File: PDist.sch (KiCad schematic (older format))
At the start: 2 parts

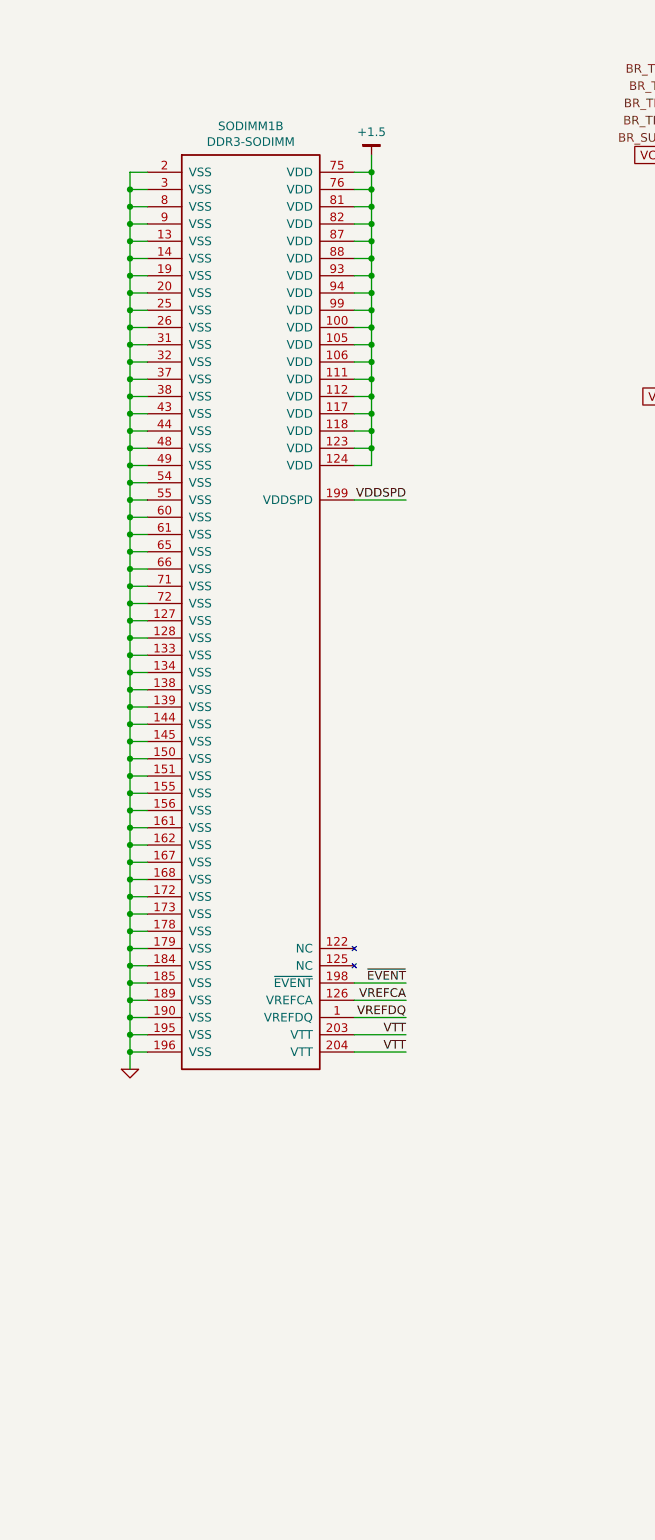
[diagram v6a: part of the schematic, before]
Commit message: Reroute SDRAM after bank swap
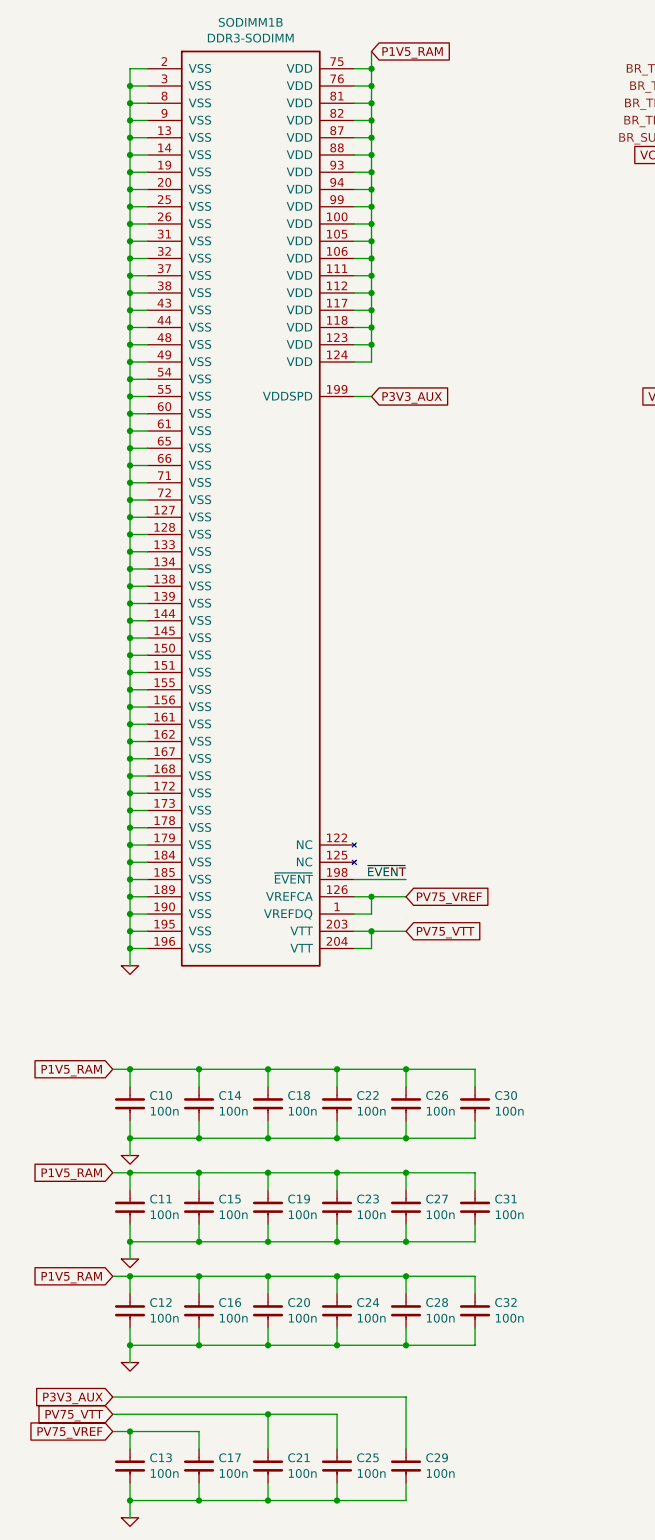
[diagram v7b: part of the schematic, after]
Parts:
- added C10, C11, C12, C13, C14, C15, C16, C17, C18, C19, C20, C21, C22, C23, C24, C25, C26, C27, C28, C29, C30, C31, C32: 100n, IPC7351-Nominal:CAPC1005X55, symbol C-0402
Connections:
- net VREFDQ is gone; now on net PV75_VREF: SODIMM1.1 (VREFDQ)
- net GND: now also C10.2, C11.2, C12.2, C13.2, C14.2, C15.2, C16.2, C17.2, C18.2, C19.2, C20.2, C21.2, C22.2, C23.2, C24.2, C25.2, C26.2, C27.2, C28.2, C29.2, C30.2, C31.2, C32.2
- net +1.5 renamed P1V5_RAM
- net P1V5_RAM: now also C10.1, C11.1, C12.1, C14.1, C15.1, C16.1, C18.1, C19.1, C20.1, C22.1, C23.1, C24.1, C26.1, C27.1, C28.1, C30.1, C31.1, C32.1
- net VDDSPD renamed P3V3_AUX
- net P3V3_AUX: now also C29.1
- net VREFCA renamed PV75_VREF
- net PV75_VREF: now also C13.1, C17.1
- net VTT renamed PV75_VTT
- net PV75_VTT: now also C21.1, C25.1
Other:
- moved on the sheet: SODIMM1B

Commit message: workworkwork
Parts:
- added CPU0, CPU1: XC6SLX25-FGG484, manuf:XILINX-FGG484, symbol XC6SLX25-FGG484
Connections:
- net GND: now also CPU0.A1 (GND), CPU0.A22 (GND), CPU0.AA13 (GND), CPU0.AA17 (GND), CPU0.AA5 (GND), CPU0.AA9 (GND), CPU0.AB1 (GND), CPU0.AB22 (GND), CPU0.B13 (GND), CPU0.B17 (GND), CPU0.B5 (GND), CPU0.B9 (GND), CPU0.D18 (GND), CPU0.D4 (GND), CPU0.E11 (GND), CPU0.E15 (GND), CPU0.E2 (GND), CPU0.E21 (GND), CPU0.E7 (GND), CPU0.G18 (GND), CPU0.G5 (GND), CPU0.H7 (GND), CPU0.J11 (GND), CPU0.J13 (GND), CPU0.J15 (GND), CPU0.J2 (GND), CPU0.J21 (GND), CPU0.J9 (GND), CPU0.K10 (GND), CPU0.K12 (GND), CPU0.K14 (GND), CPU0.L11 (GND), CPU0.L13 (GND), CPU0.L18 (GND), CPU0.L5 (GND), CPU0.L9 (GND), CPU0.M10 (GND), CPU0.M12 (GND), CPU0.M14 (GND), CPU0.N11 (GND), CPU0.N13 (GND), CPU0.N17 (GND), CPU0.N2 (GND), CPU0.N21 (GND), CPU0.N9 (GND), CPU0.P10 (GND), CPU0.P12 (GND), CPU0.P14 (GND), CPU0.R18 (GND), CPU0.R5 (GND), CPU0.U2 (GND), CPU0.U21 (GND), CPU0.U7 (GND), CPU0.V10 (GND), CPU0.V14 (GND), CPU0.V4 (GND), CPU0.W16 (GND), CPU0.W19 (GND), CPU0.W7 (GND), CPU1.A1 (GND), CPU1.A22 (GND), CPU1.AA13 (GND), CPU1.AA17 (GND), CPU1.AA5 (GND), CPU1.AA9 (GND), CPU1.AB1 (GND), CPU1.AB22 (GND), CPU1.B13 (GND), CPU1.B17 (GND), CPU1.B5 (GND), CPU1.B9 (GND), CPU1.D18 (GND), CPU1.D4 (GND), CPU1.E11 (GND), CPU1.E15 (GND), CPU1.E2 (GND), CPU1.E21 (GND), CPU1.E7 (GND), CPU1.G18 (GND), CPU1.G5 (GND), CPU1.H7 (GND), CPU1.J11 (GND), CPU1.J13 (GND), CPU1.J15 (GND), CPU1.J2 (GND), CPU1.J21 (GND), CPU1.J9 (GND), CPU1.K10 (GND), CPU1.K12 (GND), CPU1.K14 (GND), CPU1.L11 (GND), CPU1.L13 (GND), CPU1.L18 (GND), CPU1.L5 (GND), CPU1.L9 (GND), CPU1.M10 (GND), CPU1.M12 (GND), CPU1.M14 (GND), CPU1.N11 (GND), CPU1.N13 (GND), CPU1.N17 (GND), CPU1.N2 (GND), CPU1.N21 (GND), CPU1.N9 (GND), CPU1.P10 (GND), CPU1.P12 (GND), CPU1.P14 (GND), CPU1.R18 (GND), CPU1.R5 (GND), CPU1.U2 (GND), CPU1.U21 (GND), CPU1.U7 (GND), CPU1.V10 (GND), CPU1.V14 (GND), CPU1.V4 (GND), CPU1.W16 (GND), CPU1.W19 (GND), CPU1.W7 (GND)
- net VCCAUX renamed P3V3_BRIDGE
- net VCORE renamed P1V2_BRIDGE
- new net CPU0_SUSP: CPU0.N15 (SUSPEND)
- new net CPU0_TCK: CPU0.G15 (TCK)
- new net CPU0_TDI: CPU0.E18 (TDI)
- new net CPU0_TDO: CPU0.A19 (TDO)
- new net CPU0_TMS: CPU0.C18 (TMS)
- new net CPU1_SUSP: CPU1.N15 (SUSPEND)
- new net CPU1_TCK: CPU1.G15 (TCK)
- new net CPU1_TDI: CPU1.E18 (TDI)
- new net CPU1_TDO: CPU1.A19 (TDO)
- new net CPU1_TMS: CPU1.C18 (TMS)
- new net P1V2_CPU: CPU0.J10 (VCCINT), CPU0.J12 (VCCINT), CPU0.J14 (VCCINT), CPU0.J8 (VCCINT), CPU0.K11 (VCCINT), CPU0.K13 (VCCINT), CPU0.K9 (VCCINT), CPU0.L10 (VCCINT), CPU0.L12 (VCCINT), CPU0.L14 (VCCINT), CPU0.M11 (VCCINT), CPU0.M13 (VCCINT), CPU0.M9 (VCCINT), CPU0.N10 (VCCINT), CPU0.N12 (VCCINT), CPU0.N14 (VCCINT), CPU0.P11 (VCCINT), CPU0.P13 (VCCINT), CPU0.P9 (VCCINT), CPU0.R14 (VCCINT), CPU1.J10 (VCCINT), CPU1.J12 (VCCINT), CPU1.J14 (VCCINT), CPU1.J8 (VCCINT), CPU1.K11 (VCCINT), CPU1.K13 (VCCINT), CPU1.K9 (VCCINT), CPU1.L10 (VCCINT), CPU1.L12 (VCCINT), CPU1.L14 (VCCINT), CPU1.M11 (VCCINT), CPU1.M13 (VCCINT), CPU1.M9 (VCCINT), CPU1.N10 (VCCINT), CPU1.N12 (VCCINT), CPU1.N14 (VCCINT), CPU1.P11 (VCCINT), CPU1.P13 (VCCINT), CPU1.P9 (VCCINT), CPU1.R14 (VCCINT)
- new net P3V3_CPU: CPU0.D16 (VCCAUX), CPU0.F11 (VCCAUX), CPU0.G12 (VCCAUX), CPU0.H15 (VCCAUX), CPU0.H9 (VCCAUX), CPU0.K15 (VCCAUX), CPU0.L8 (VCCAUX), CPU0.M15 (VCCAUX), CPU0.N8 (VCCAUX), CPU0.R10 (VCCAUX), CPU0.R12 (VCCAUX), CPU0.R6 (VCCAUX), CPU0.U11 (VCCAUX), CPU0.V6 (VCCAUX), CPU1.D16 (VCCAUX), CPU1.F11 (VCCAUX), CPU1.G12 (VCCAUX), CPU1.H15 (VCCAUX), CPU1.H9 (VCCAUX), CPU1.K15 (VCCAUX), CPU1.L8 (VCCAUX), CPU1.M15 (VCCAUX), CPU1.N8 (VCCAUX), CPU1.R10 (VCCAUX), CPU1.R12 (VCCAUX), CPU1.R6 (VCCAUX), CPU1.U11 (VCCAUX), CPU1.V6 (VCCAUX)
